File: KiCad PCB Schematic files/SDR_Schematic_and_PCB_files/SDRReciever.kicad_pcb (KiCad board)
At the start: 2 copper layers, 83 x 34.7 mm, 66 parts, among them J1 Conn_Coaxial, J10 I_0, J11 I_180, J12 Q_90, J13 Q_270, J14 AudioJack3, J2 3.3V, J3 FIL_IN, J4 5V, J5 4.3V, J6 FIL_OUT, J7 CLK_2, J8 CLK_0, J9 CLK_1, Q1 MMBT2222A-TP, Q2 BSS138, Q3 BSS138, U1 Si5351A-B-GT, U2 SN74CBT3253, U3 LM4562, Y1 CX3225SB

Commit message: Revised PCB part placement
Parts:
- moved R9 25.8 mm to (133.4, 139.4), turned to 270 degrees
- moved C7 24.5 mm to (139.9, 128.5), turned to 0 degrees
- moved R8 24.1 mm to (126.5, 139.2), turned to 270 degrees
- moved R12 20.8 mm to (116.1, 138.8), turned to 270 degrees
- moved R10 19.8 mm to (128.9, 139.3), turned to 270 degrees
- moved R11 19.3 mm to (131.0, 139.4), turned to 270 degrees
- moved JP1 18.4 mm to (116.6, 118.4), turned to 270 degrees
- moved J7 17.7 mm to (152.2, 146.7)
- moved J8 17.7 mm to (159.4, 146.7)
- moved J9 17.7 mm to (155.8, 146.7)
- moved C16 17.7 mm to (121.1, 118.2), turned to 90 degrees
- moved R13 17.4 mm to (119.7, 138.8), turned to 270 degrees
- moved Y1 17.2 mm to (146.9, 146.0)
- moved C10 17.0 mm to (115.5, 133.4), turned to 90 degrees
- moved J10 16.3 mm to (114.4, 129.6)
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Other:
- board size 83 x 34.7 mm -> 85.8 x 35 mm

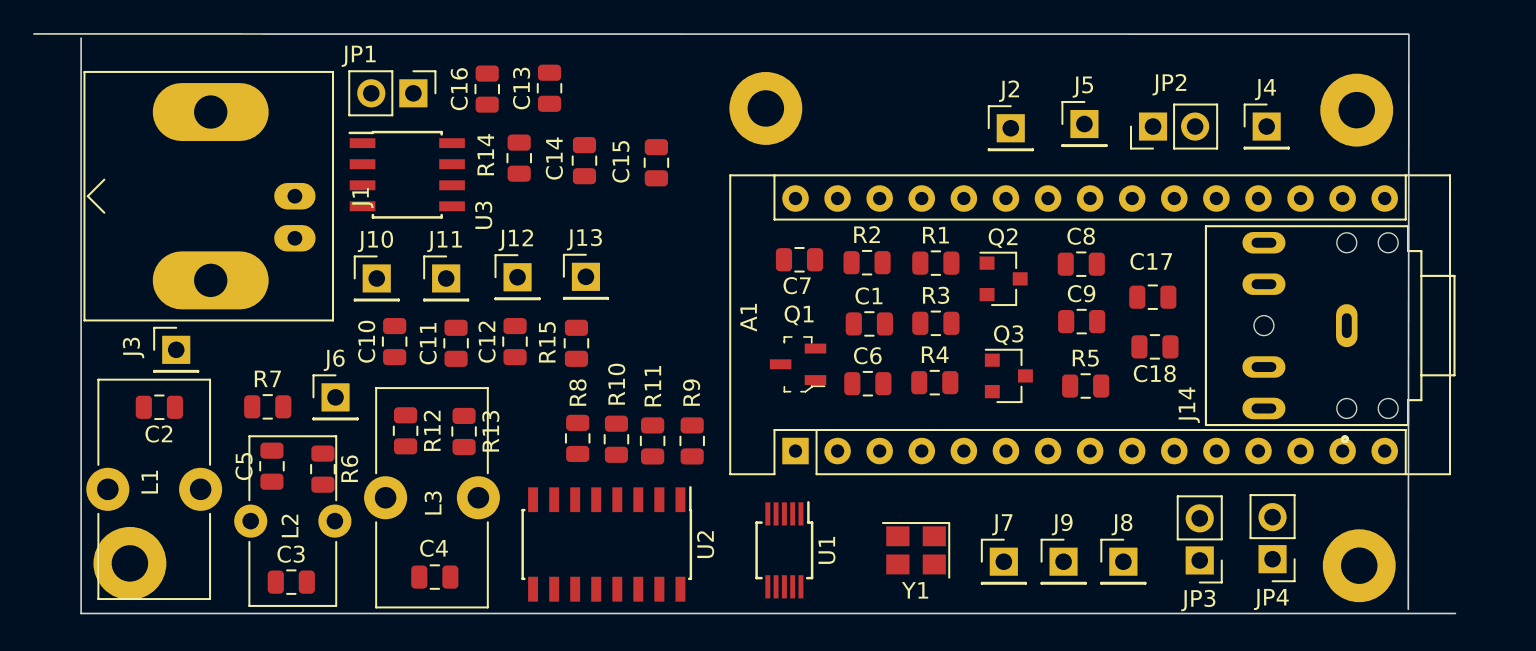
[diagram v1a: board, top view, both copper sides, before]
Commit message: Revised placement of PCB parts
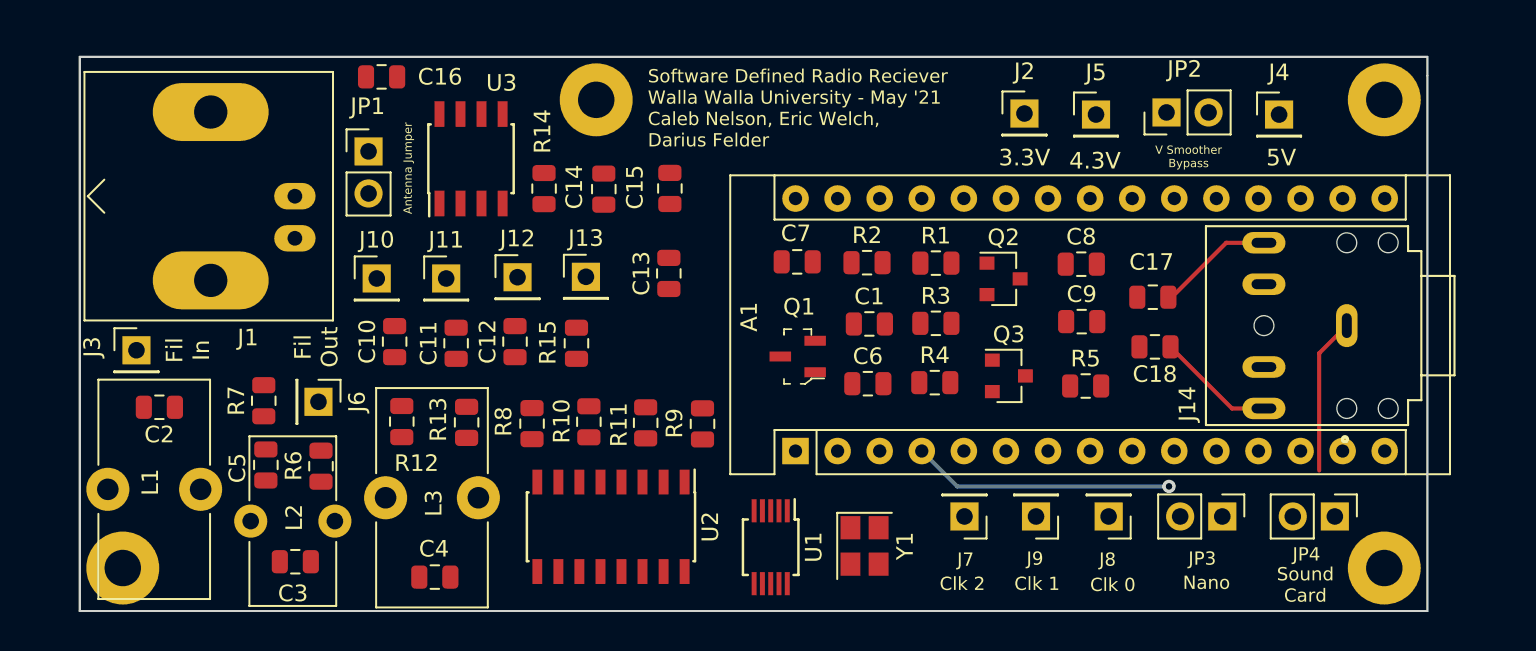
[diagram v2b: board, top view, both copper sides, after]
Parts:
- moved C13 13.3 mm to (132.0, 129.3)
- moved H3 10.2 mm to (127.6, 118.8)
- moved C16 6.42 mm to (114.7, 117.4), turned to 180 degrees
- moved JP4 4.56 mm to (172.2, 144.0), turned to 270 degrees
- moved JP1 4.43 mm to (113.9, 121.9), turned to 0 degrees
- moved U3 3.97 mm to (120.1, 122.4), turned to 90 degrees
- moved J7 3.62 mm to (149.9, 144.0), turned to 180 degrees
- moved J9 3.20 mm to (154.2, 144.0), turned to 180 degrees
- moved Y1 3.12 mm to (143.8, 145.7), turned to 270 degrees
- moved JP3 2.98 mm to (165.4, 144.0), turned to 270 degrees
- moved R8 2.90 mm to (123.8, 138.4)
- moved J8 2.87 mm to (158.6, 144.0), turned to 180 degrees
- moved J3 2.40 mm to (99.9, 133.9)
- moved R14 2.37 mm to (124.5, 124.2)
- moved C14 2.08 mm to (128.1, 124.2)
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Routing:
- net Net-(A1-Pad29): track 0.00 -> 15.9 mm, vias 0 -> 1
- net Net-(J14-Pad1): track 0.00 -> 9.43 mm
- net Net-(C18-Pad1): track 0.00 -> 7.18 mm
- net Net-(C17-Pad1): track 0.00 -> 7.13 mm
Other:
- board size 85.8 x 35 mm -> 81.3 x 33.5 mm
- board text added: "3.3V"
- board text added: "4.3V"
- board text added: "5V"
- board text added: "Antenna Jumper"
- board text added: "Clk 0"
- board text added: "Clk 1"
- board text added: "Clk 2"
- board text added: "Fil In"
- board text added: "Fil Out"
- board text added: "Nano"
- board text added: "Software Defined Radio Reciever Walla Walla University - May '21 Caleb Nelson, Eric Welch, Darius Felder"
- board text added: "Sound Card"
- board text added: "V Smoother Bypass"

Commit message: Initial PCB tracing complete
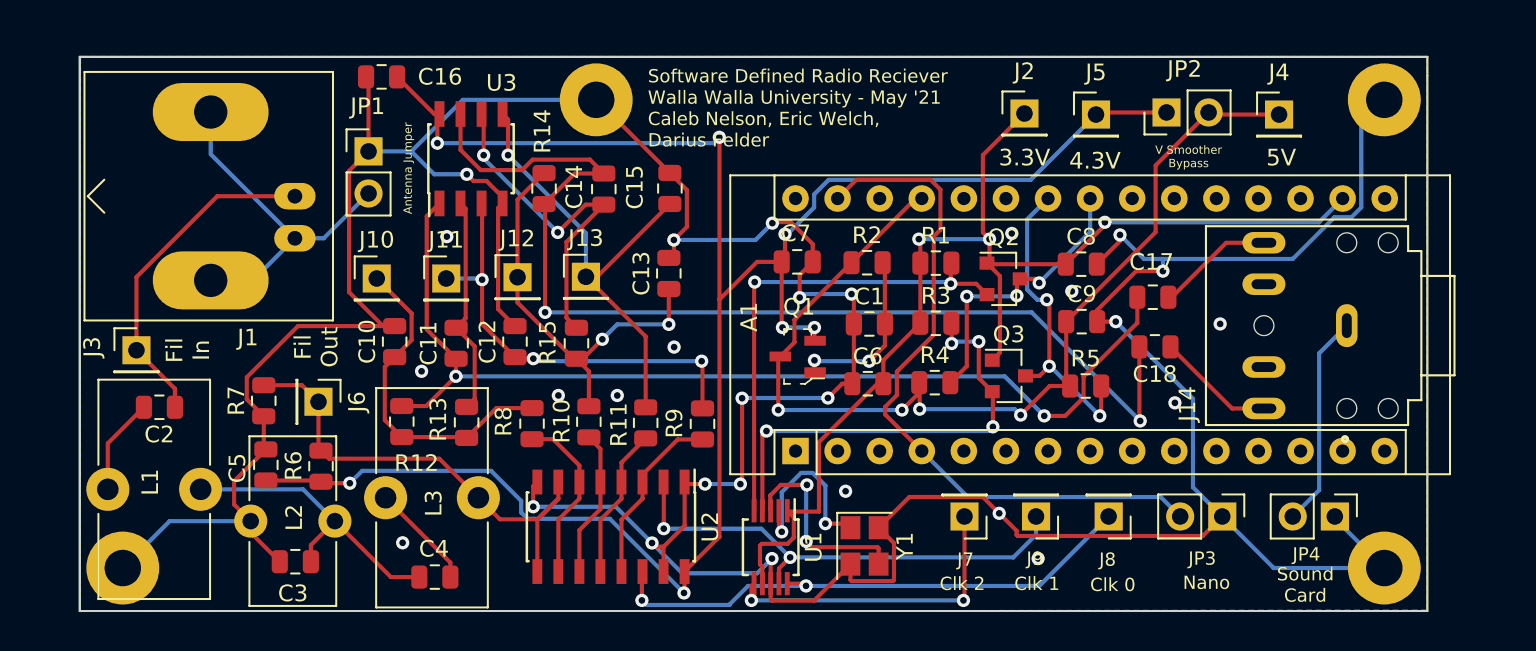
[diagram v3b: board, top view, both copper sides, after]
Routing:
- net GND: track 0.00 -> 256.0 mm, vias 0 -> 28
- net +4.3V: track 0.00 -> 119.8 mm, vias 0 -> 7
- net +3V3: track 0.00 -> 71.7 mm, vias 0 -> 3
- net Net-(C14-Pad1): track 0.00 -> 66.0 mm, vias 0 -> 2
- net Net-(C11-Pad1): track 0.00 -> 62.2 mm, vias 0 -> 2
- net +5V: track 0.00 -> 62.2 mm, vias 0 -> 4
- net /I_LO: track 0.00 -> 33.5 mm, vias 0 -> 2
- net /Q_LO: track 0.00 -> 29.5 mm, vias 0 -> 2
- net /SDA_3V: track 0.00 -> 29.4 mm, vias 0 -> 2
- net /BPF_OUT: track 0.00 -> 29.2 mm
- net Net-(C15-Pad1): track 0.00 -> 28.2 mm, vias 0 -> 1
- net /SCL_3V: track 0.00 -> 27.1 mm, vias 0 -> 4
- net Net-(C12-Pad1): track 0.00 -> 26.5 mm, vias 0 -> 3
- net Net-(A1-Pad29): track 15.9 -> 42.2 mm, vias 1 -> 0
- net Net-(C13-Pad1): track 0.00 -> 25.2 mm, vias 0 -> 2
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- added copper zone on B.Cu, net GND
- added copper zone on F.Cu, net GND

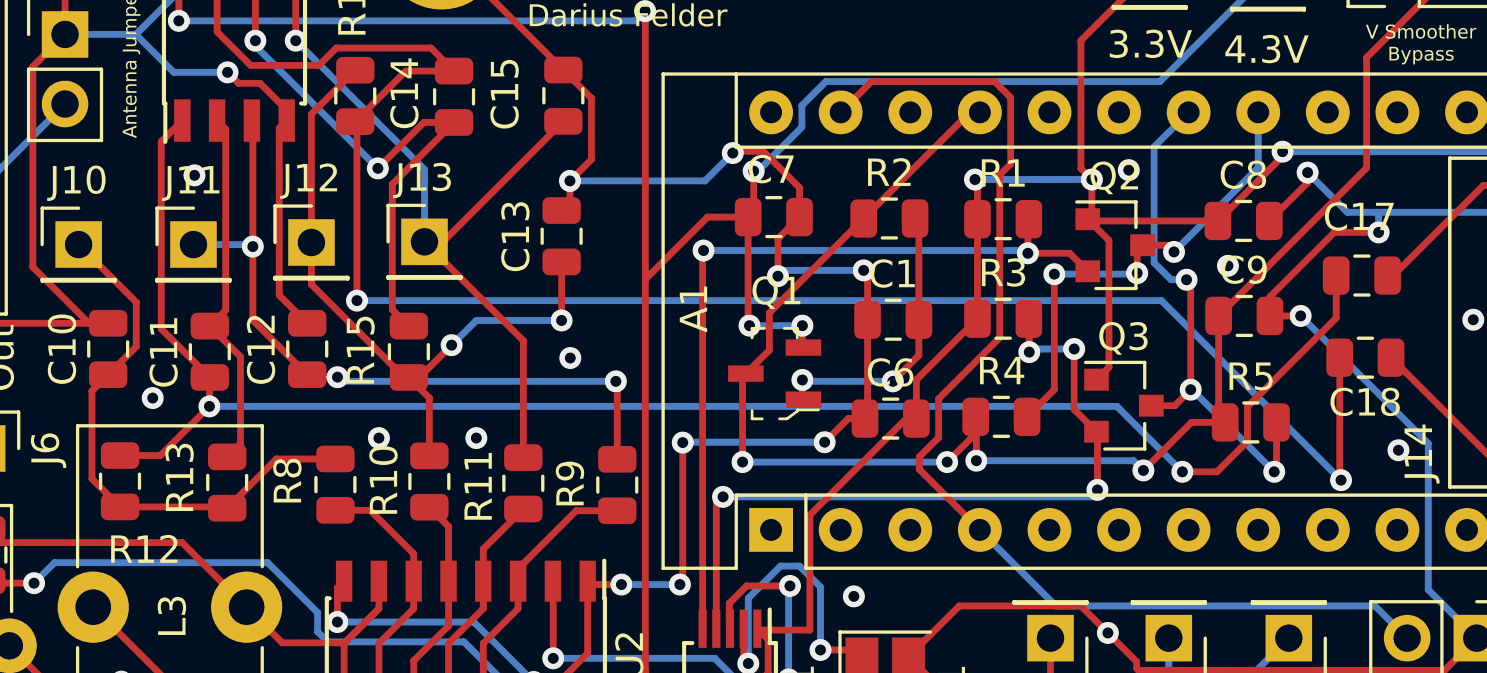
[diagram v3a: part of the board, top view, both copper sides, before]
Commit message: Added more vias to improve ground plane on PCB
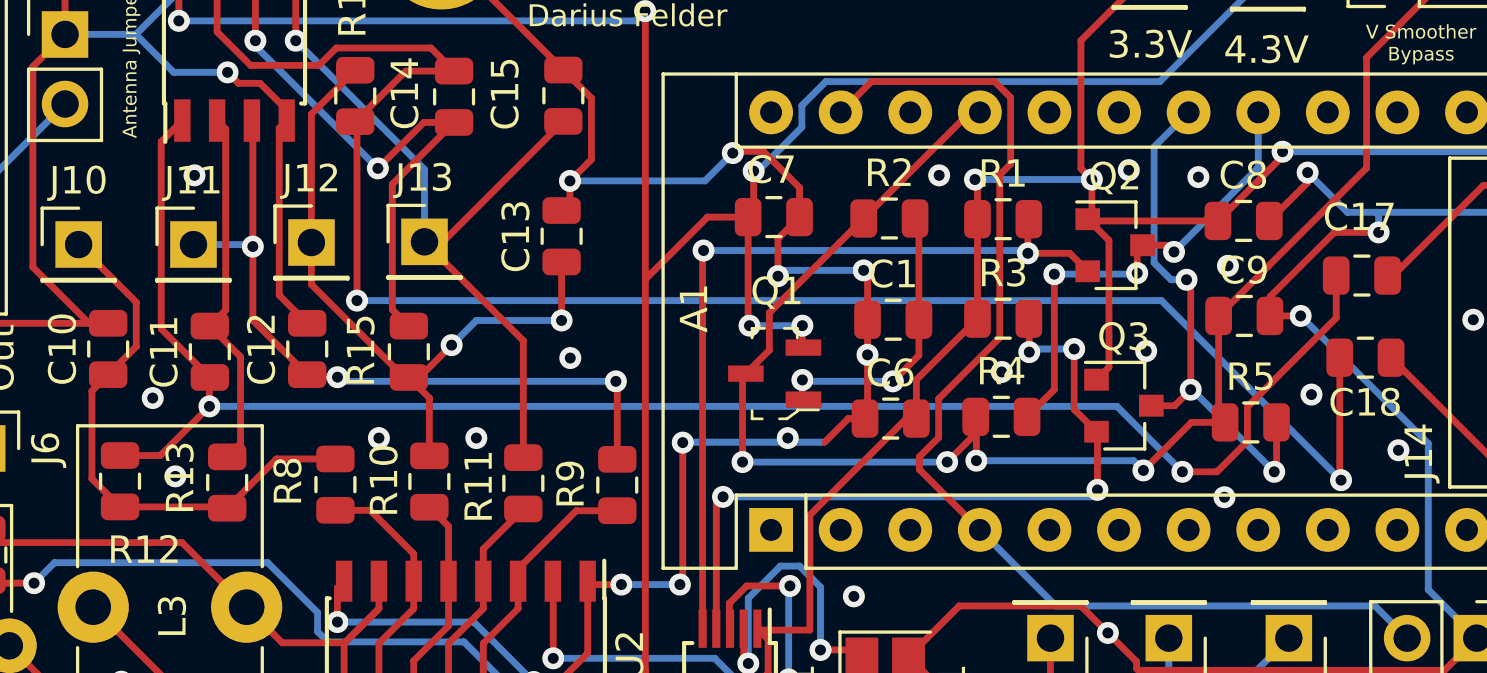
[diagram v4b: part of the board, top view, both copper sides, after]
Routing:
- net GND: vias 28 -> 36

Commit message: Revision 1 complete First complete PCB design.
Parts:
- I 0: renamed from J10
- I 180: renamed from J11
- Q 270: renamed from J13
- Q 90: renamed from J12
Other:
- board size 81.3 x 33.5 mm -> 81.3 x 33.7 mm
- board text added: "Arduino"
- board text added: "Audio"
- board text added: "Designed By: Caleb Nelson, Darius Felder, Eric Walsh"
- board text added: "Software Defined Radio Reciever Walla Walla University Revision 1"
- board text added: "USB <--"
- board text removed: "Nano"
- board text removed: "Sound Card"

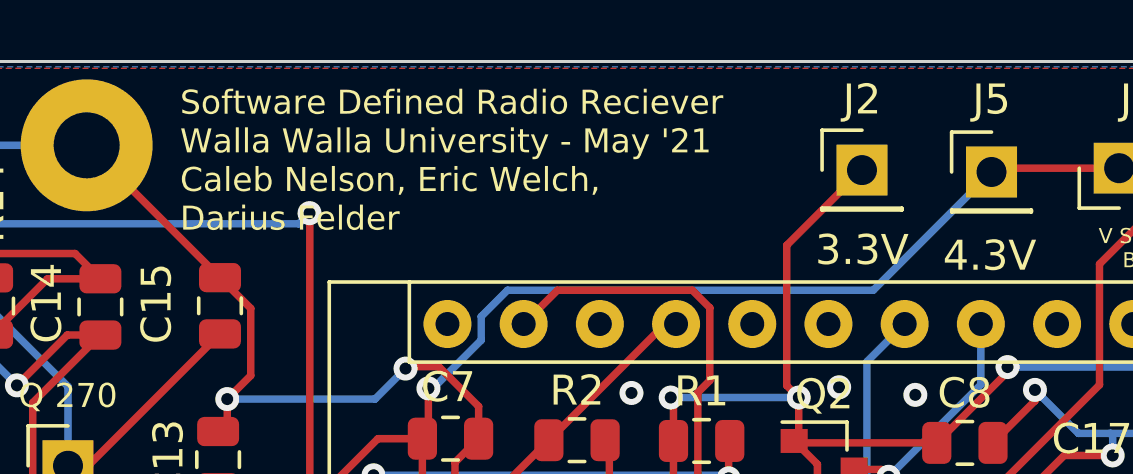
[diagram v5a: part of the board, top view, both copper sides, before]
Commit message: PCB revision 1 complete. Added 3D model and updated silk screen.
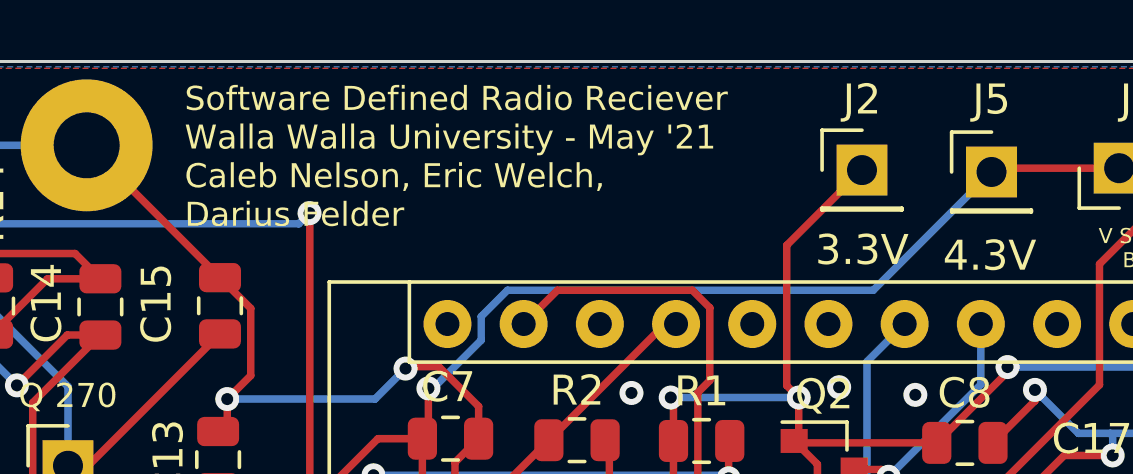
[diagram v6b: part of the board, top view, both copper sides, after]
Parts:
- added G***: LOGO, Imported_Footprints:Dolphin, F.Cu at (101.9, 125.9)
